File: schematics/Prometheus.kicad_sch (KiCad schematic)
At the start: 15 parts, among them J1 ATX Power Conn, SW1 Power Switch, SW2 Reset Switch, U1 DS1501YN, U2 wdc65c816, X1 32kHz, X2 8MHz

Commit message: Small tweaks here and there. Added a lot of missing footprint definitions.
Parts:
- BT1: footprint (none) -> Battery:BatteryHolder_Keystone_1058_1x2032
- C1, C2: footprint (none) -> Capacitor_THT:CP_Radial_D4.0mm_P1.50mm
- R1, R2, R3, R4: footprint Resistor_THT:R_Axial_DIN0411_L9.9mm_D3.6mm_P12.70mm_Horizontal -> Resistor_SMD:R_0805_2012Metric_Pad1.20x1.40mm_HandSolder
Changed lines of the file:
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@@
 	(label "A0"
 		(at 218.44 46.99 0)
-		(fields_autoplaced yes)
 		(effects
 			(font
@@
 	(label "A8"
 		(at 218.44 67.31 0)
-		(fields_autoplaced yes)
 		(effects
 			(font
@@
 	(label "A3"
 		(at 218.44 54.61 0)
-		(fields_autoplaced yes)
 		(effects
 			(font
@@
 	(label "A3"
 		(at 149.86 41.91 0)
-		(fields_autoplaced yes)
 		(effects
 			(font
@@
 	(label "D2"
 		(at 149.86 57.15 0)
-		(fields_autoplaced yes)
 		(effects
 			(font
@@
 	(label "D4"
 		(at 173.99 57.15 0)
-		(fields_autoplaced yes)
 		(effects
 			(font
@@
 	(label "D7"
 		(at 250.19 62.23 0)
-		(fields_autoplaced yes)
 		(effects
 			(font
@@
 	(label "D7"
 		(at 173.99 49.53 0)
-		(fields_autoplaced yes)
 		(effects
 			(font
@@
 	(label "A4"
 		(at 218.44 57.15 0)
-		(fields_autoplaced yes)
 		(effects
 			(font
@@
 	(label "A7"
 		(at 218.44 64.77 0)
-		(fields_autoplaced yes)
 		(effects
 			(font
@@
 	(label "D5"
 		(at 173.99 54.61 0)
-		(fields_autoplaced yes)
 		(effects
 			(font
@@
 	(label "A12"
 		(at 247.65 72.39 0)
-		(fields_autoplaced yes)
 		(effects
 			(font
@@
 	(label "D3"
 		(at 250.19 52.07 0)
-		(fields_autoplaced yes)
 		(effects
 			(font
@@
 	(label "D3"
 		(at 173.99 59.69 0)
-		(fields_autoplaced yes)
 		(effects
 			(font
@@
 	(label "A4"
 		(at 149.86 39.37 0)
-		(fields_autoplaced yes)
 		(effects
 			(font
@@
 	(label "A5"
 		(at 218.44 59.69 0)
-		(fields_autoplaced yes)
 		(effects
 			(font
@@
 	(label "A9"
 		(at 218.44 69.85 0)
-		(fields_autoplaced yes)
 		(effects
 			(font
@@
 	(label "A10"
 		(at 218.44 72.39 0)
-		(fields_autoplaced yes)
 		(effects
 			(font
@@
 	(label "D2"
 		(at 250.19 49.53 0)
-		(fields_autoplaced yes)
 		(effects
 			(font
@@
 	(label "A1"
 		(at 149.86 46.99 0)
-		(fields_autoplaced yes)
 		(effects
 			(font
@@
 	(label "A15"
 		(at 247.65 64.77 0)
-		(fields_autoplaced yes)
 		(effects
 			(font
@@
 	(label "D0"
 		(at 250.19 44.45 0)
-		(fields_autoplaced yes)
 		(effects
 			(font
@@
 	(label "D0"
 		(at 149.86 52.07 0)
-		(fields_autoplaced yes)
 		(effects
 			(font
@@
 	(label "A0"
 		(at 149.86 49.53 0)
-		(fields_autoplaced yes)
 		(effects
 			(font
@@
 	(label "D6"
 		(at 250.19 59.69 0)
-		(fields_autoplaced yes)
 		(effects
 			(font
@@
 	(label "D1"
 		(at 149.86 54.61 0)
-		(fields_autoplaced yes)
 		(effects
 			(font
@@
 	(label "A11"
 		(at 218.44 74.93 0)
-		(fields_autoplaced yes)
 		(effects
 			(font
@@
 	(label "D6"
 		(at 173.99 52.07 0)
-		(fields_autoplaced yes)
 		(effects
 			(font
@@
 	(label "D1"
 		(at 250.19 46.99 0)
-		(fields_autoplaced yes)
 		(effects
 			(font
@@
 	(label "A1"
 		(at 218.44 49.53 0)
-		(fields_autoplaced yes)
 		(effects
 			(font
@@
 	(label "A6"
 		(at 218.44 62.23 0)
-		(fields_autoplaced yes)
 		(effects
 			(font
@@
 	(label "A2"
 		(at 218.44 52.07 0)
-		(fields_autoplaced yes)
 		(effects
 			(font
@@
 	(label "D5"
 		(at 250.19 57.15 0)
-		(fields_autoplaced yes)
 		(effects
 			(font
@@
 	(label "A13"
 		(at 247.65 69.85 0)
-		(fields_autoplaced yes)
 		(effects
 			(font
@@
 	(label "A14"
 		(at 247.65 67.31 0)
-		(fields_autoplaced yes)
 		(effects
 			(font
@@
 	(label "D4"
 		(at 250.19 54.61 0)
-		(fields_autoplaced yes)
 		(effects
 			(font
@@
 	(label "A2"
 		(at 149.86 44.45 0)
-		(fields_autoplaced yes)
 		(effects
 			(font
@@
 			)
 		)
-		(property "Footprint" ""
+		(property "Footprint" "Battery:BatteryHolder_Keystone_1058_1x2032"
 			(at 187.706 34.29 90)
 			(effects
@@
 			)
 		)
-		(property "Footprint" "Resistor_THT:R_Axial_DIN0411_L9.9mm_D3.6mm_P12.70mm_Horizontal"
+		(property "Footprint" "Resistor_SMD:R_0805_2012Metric_Pad1.20x1.40mm_HandSolder"
 			(at 212.09 144.018 90)
 			(effects
@@
 			)
 		)
-		(property "Footprint" "Resistor_THT:R_Axial_DIN0411_L9.9mm_D3.6mm_P12.70mm_Horizontal"
+		(property "Footprint" "Resistor_SMD:R_0805_2012Metric_Pad1.20x1.40mm_HandSolder"
 			(at 178.562 149.86 90)
 			(effects
@@
 			)
 		)
-		(property "Footprint" "Resistor_THT:R_Axial_DIN0411_L9.9mm_D3.6mm_P12.70mm_Horizontal"
+		(property "Footprint" "Resistor_SMD:R_0805_2012Metric_Pad1.20x1.40mm_HandSolder"
 			(at 189.992 149.86 90)
 			(effects
@@
 			)
 		)
-		(property "Footprint" "Resistor_THT:R_Axial_DIN0411_L9.9mm_D3.6mm_P12.70mm_Horizontal"
+		(property "Footprint" "Resistor_SMD:R_0805_2012Metric_Pad1.20x1.40mm_HandSolder"
 			(at 202.692 149.86 90)
 			(effects
@@
 			)
 		)
-		(property "Footprint" ""
+		(property "Footprint" "Capacitor_THT:CP_Radial_D4.0mm_P1.50mm"
 			(at 271.4752 160.02 0)
 			(effects
@@
 			)
 		)
-		(property "Footprint" ""
+		(property "Footprint" "Capacitor_THT:CP_Radial_D4.0mm_P1.50mm"
 			(at 258.7752 160.02 0)
 			(effects

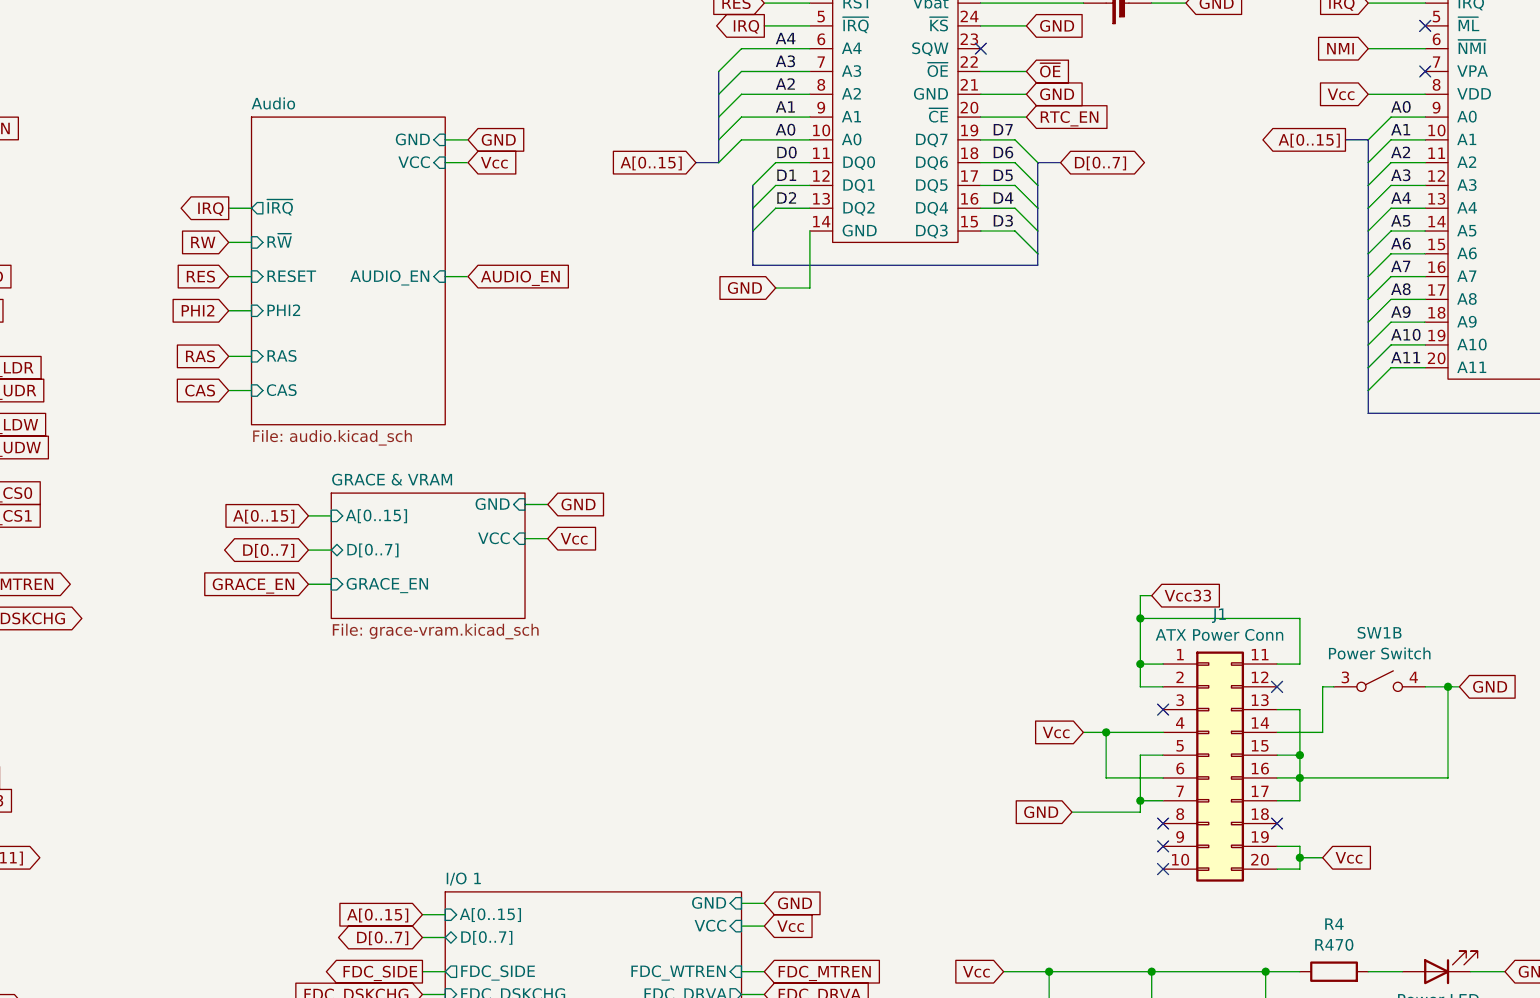
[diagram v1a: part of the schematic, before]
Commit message: Added analog audio section. Followed Apple IIGS schematics for this one as it uses the same EN5503DOC audio chip. Still a bit unclear how to connect the RCA jacks instead of the phonejack and analog ground is not connected.
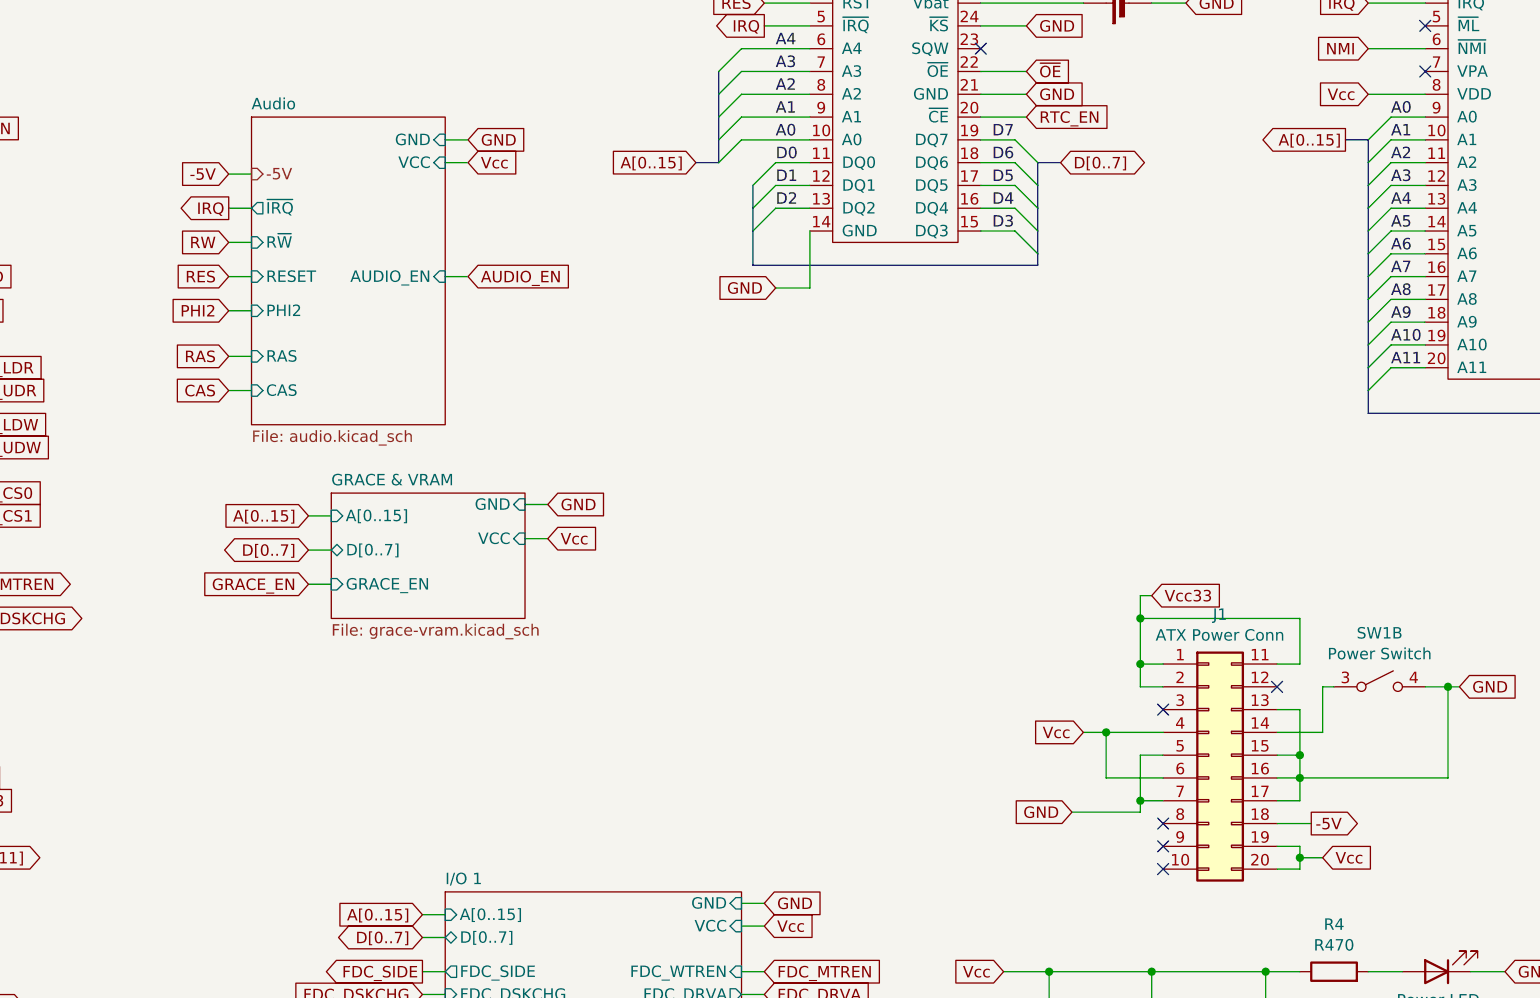
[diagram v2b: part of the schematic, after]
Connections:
- net -5V : now reaches J1.18 (Pin_18)
- no-connect marks 19 -> 18
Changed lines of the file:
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@@
 	)
 	(no_connect
-		(at 205.74 125.73)
-	)
-	(no_connect
 		(at 222.25 41.91)
 	)
@@
 	(wire
 		(pts
+			(xy 205.74 125.73) (xy 209.55 125.73)
+		)
+		(stroke
+			(width 0)
+			(type default)
+		)
+	)
+	(wire
+		(pts
 			(xy 248.92 160.02) (xy 257.81 160.02)
 		)
@@
 	(wire
 		(pts
+			(xy 88.9 53.34) (xy 91.44 53.34)
+		)
+		(stroke
+			(width 0)
+			(type default)
+		)
+	)
+	(wire
+		(pts
 			(xy 190.5 123.19) (xy 190.5 124.46)
 		)
@@
 		)
 	)
+	(global_label "-5V"
+		(shape input)
+		(at 88.9 53.34 180)
+		(fields_autoplaced yes)
+		(effects
+			(font
+				(size 1.27 1.27)
+			)
+			(justify right)
+		)
+		(property "Intersheetrefs" "${INTERSHEET_REFS}"
+			(at 82.6985 53.34 0)
+			(effects
+				(font
+					(size 1.27 1.27)
+				)
+				(justify right)
+				(hide yes)
+			)
+		)
+	)
 	(global_label "D[0..7]"
 		(shape bidirectional)
@@
 		)
 	)
+	(global_label "-5V "
+		(shape output)
+		(at 209.55 125.73 0)
+		(fields_autoplaced yes)
+		(effects
+			(font
+				(size 1.27 1.27)
+			)
+			(justify left)
+		)
+		(property "Intersheetrefs" "${INTERSHEET_REFS}"
+			(at 216.7191 125.73 0)
+			(effects
+				(font
+					(size 1.27 1.27)
+				)
+				(justify left)
+				(hide yes)
+			)
+		)
+	)
 	(global_label "GND"
 		(shape input)
@@
 		)
 	)
+	(hierarchical_label "-5V"
+		(shape output)
+		(at 91.44 53.34 0)
+		(effects
+			(font
+				(size 1.27 1.27)
+			)
+			(justify left)
+		)
+	)
